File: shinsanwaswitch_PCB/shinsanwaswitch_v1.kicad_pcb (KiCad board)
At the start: 2 copper layers, 26.3 x 15.4 mm, 9 parts, among them J1 Conn_01x05_Male, Q1 2SC5395

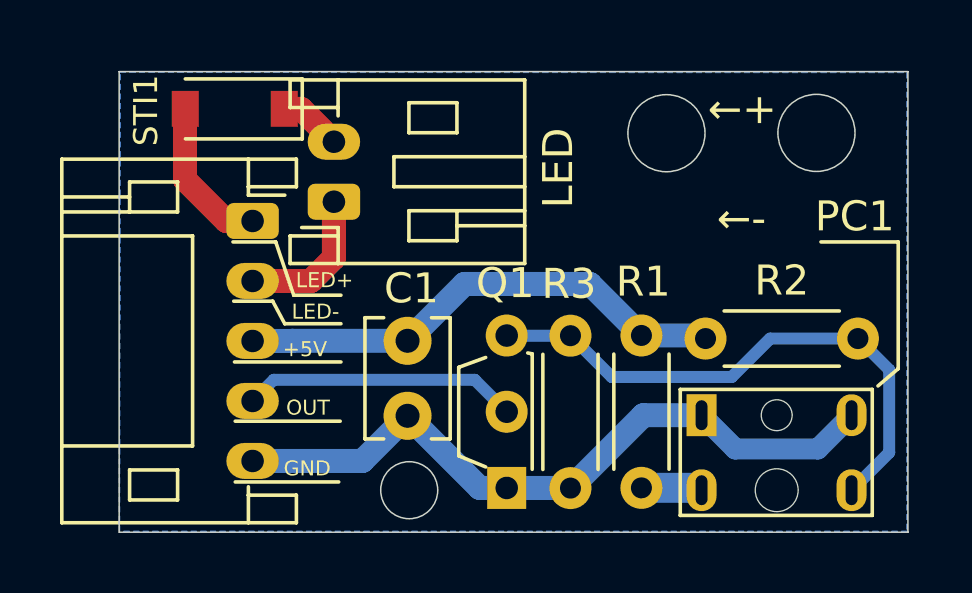
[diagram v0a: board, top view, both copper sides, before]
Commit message: Update to Kicad 6.99 + RPI-352 footprint
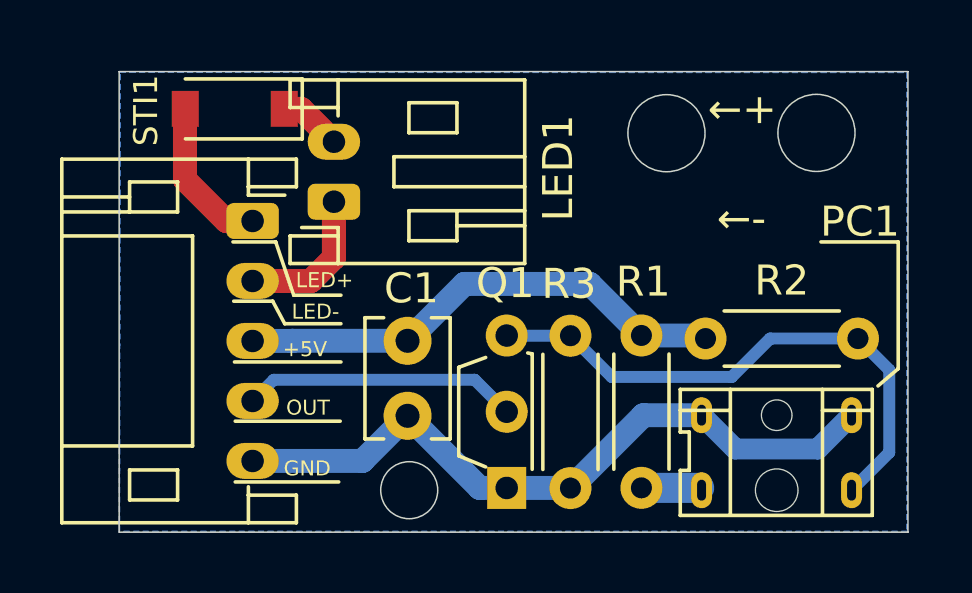
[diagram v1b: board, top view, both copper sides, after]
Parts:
- renumbered LED to LED1
